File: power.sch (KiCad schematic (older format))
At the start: 11 parts

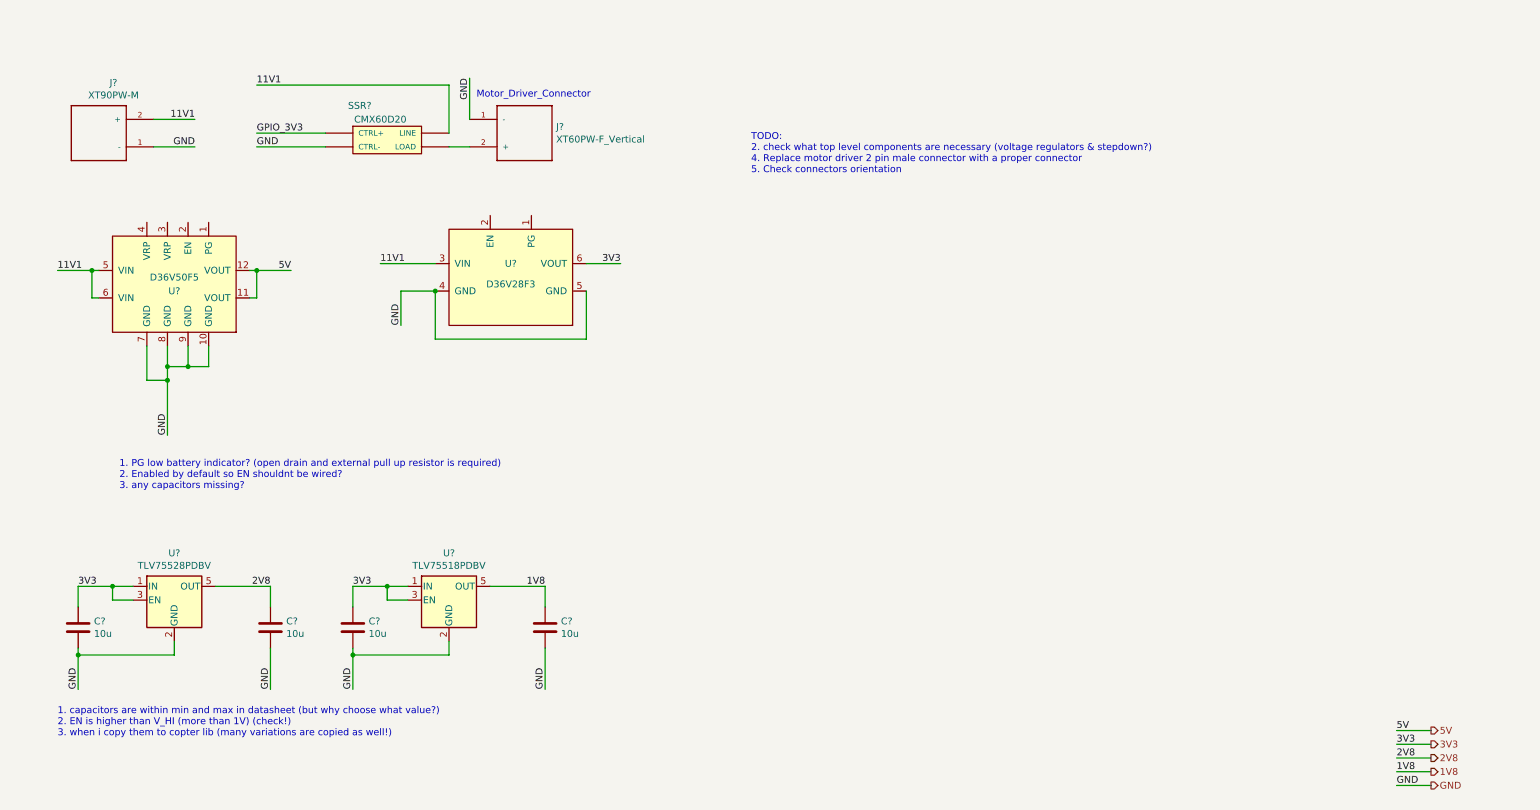
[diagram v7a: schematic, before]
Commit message: added level shifters
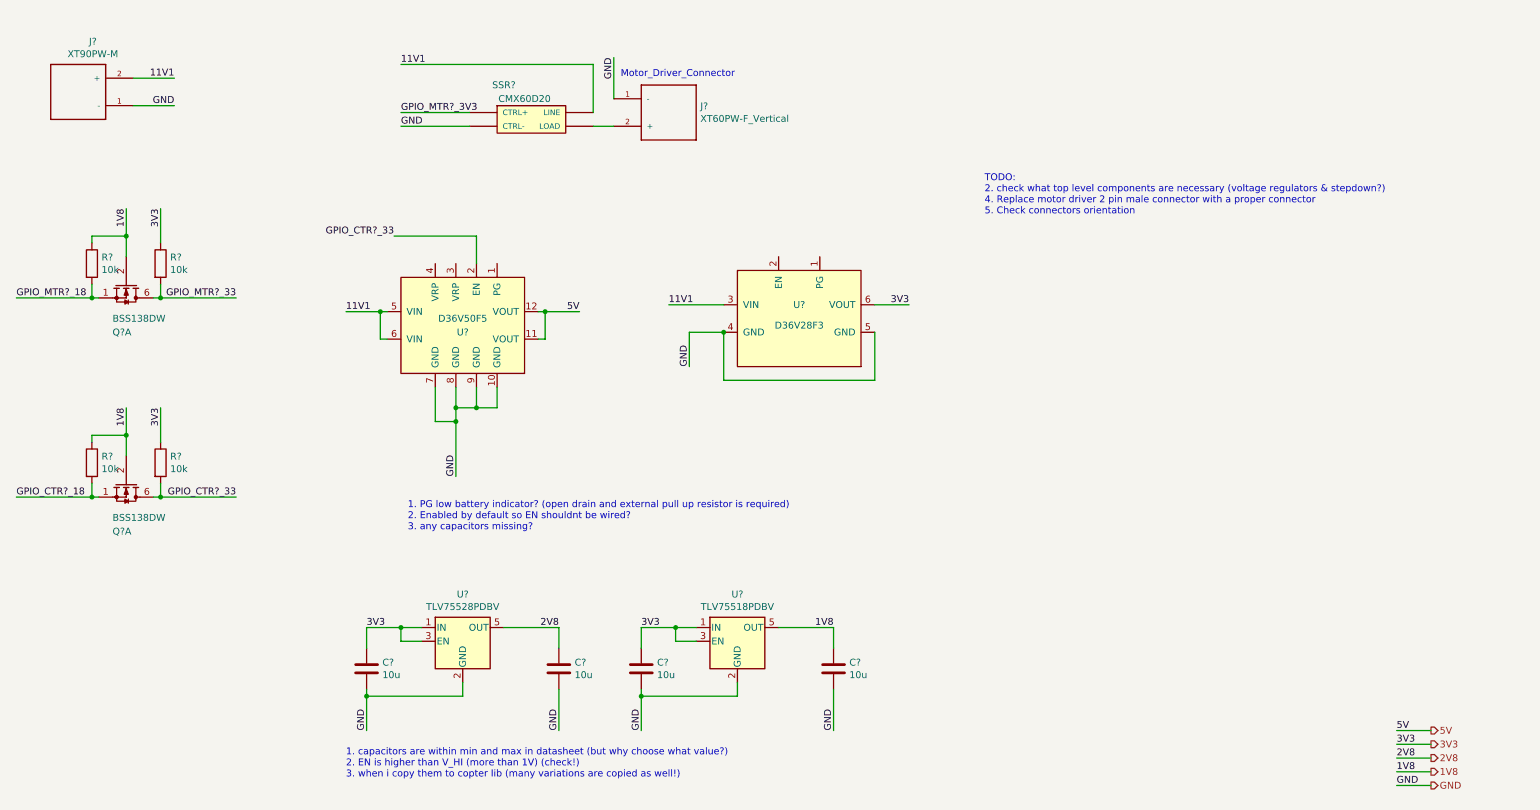
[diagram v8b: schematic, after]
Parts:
- added Q? (x2): BSS138DW, symbol Drone:BSS138DW
- added R? (x4): 10k, Resistor_SMD:R_0805_2012Metric_Pad1.15x1.40mm_HandSolder, symbol Drone:RES
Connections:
- net 1V8: now also Q?.2 (G2), Q?.2 (G2), R?.1, R?.1
- net 3V3: now also R?.1, R?.1
- net GPIO_CTR?_33: now reaches U?.2 (EN)
- net GPIO_CTR?_33: now also Q?.6 (D2), R?.2
- net GPIO_3V3 renamed GPIO_MTR?_3V3
- new net GPIO_CTR?_18: Q?.1 (S2), R?.2
- new net GPIO_MTR?_18: Q?.1 (S2), R?.2
- new net GPIO_MTR?_33: Q?.6 (D2), R?.2
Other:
- moved on the sheet: C?, J?, SSR?, U?
